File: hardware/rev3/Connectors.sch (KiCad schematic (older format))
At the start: 2 parts, among them J2 CONN_02X09, J3 CONN_02X09

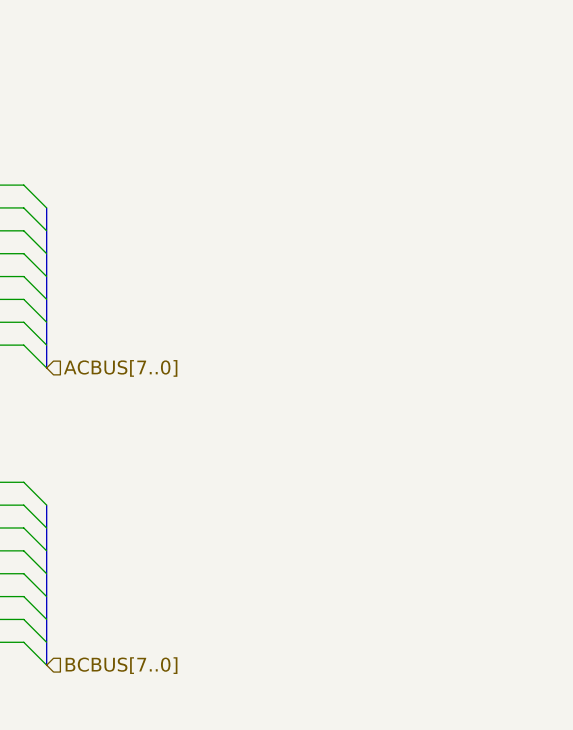
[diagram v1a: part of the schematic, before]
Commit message: Add initial output amplifier design.
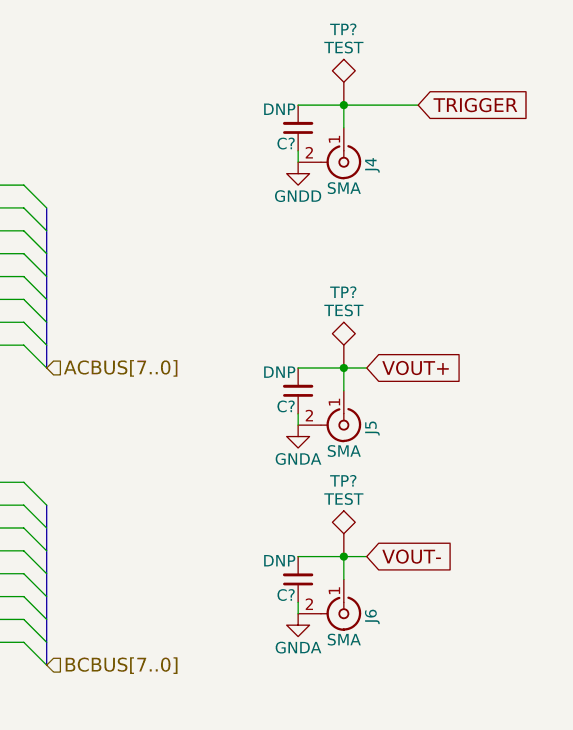
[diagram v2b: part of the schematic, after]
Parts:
- added C? (x3): DNP, symbol C_Small
- added J4, J5, J6: SMA, symbol CONN_COAXIAL
- added TP? (x3): TEST, symbol TEST
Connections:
- net GNDD: now also C?.1, J4.2 (Ext)
- new net GNDA: C?.1, C?.1, J5.2 (Ext), J6.2 (Ext)
- new net TRIGGER: C?.2, J4.1 (In), TP?.1
- new net VOUT+: C?.2, J5.1 (In), TP?.1
- new net VOUT-: C?.2, J6.1 (In), TP?.1
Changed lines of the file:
@@
 LIBS:transistors
 LIBS:conn
-LIBS:linear
 LIBS:regul
 LIBS:74xx
@@
 LIBS:AD9102
 LIBS:LMK61XX
+LIBS:linear
+LIBS:ltc6409
 LIBS:rev3-cache
 EELAYER 25 0
@@
 Text Label 2350 1350 0    60   ~ 0
 ACBUS0
+$Comp
+L CONN_COAXIAL J4
+U 1 1 58FD5BE5
+P 4250 1250
+F 0 "J4" H 4260 1370 50  0000 C CNN
+F 1 "SMA" V 4365 1250 50  0000 C CNN
+F 2 "" H 4250 1250 50  0001 C CNN
+F 3 "" H 4250 1250 50  0001 C CNN
+	1    4250 1250
+	0    1    1    0
+$EndComp
+$Comp
+L CONN_COAXIAL J5
+U 1 1 58FD5DAF
+P 4250 2400
+F 0 "J5" H 4260 2520 50  0000 C CNN
+F 1 "SMA" V 4365 2400 50  0000 C CNN
+F 2 "" H 4250 2400 50  0001 C CNN
+F 3 "" H 4250 2400 50  0001 C CNN
+	1    4250 2400
+	0    1    1    0
+$EndComp
+Text GLabel 4575 1000 2    60   Input ~ 0
+TRIGGER
+Wire Wire Line
+	4050 1000 4575 1000
+Wire Wire Line
+	4250 1000 4250 1100
+Text GLabel 4350 2150 2    60   Input ~ 0
+VOUT+
+Wire Wire Line
+	4050 2150 4350 2150
+Wire Wire Line
+	4250 2150 4250 2250
+$Comp
+L CONN_COAXIAL J6
+U 1 1 58FD62C2
+P 4250 3225
+F 0 "J6" H 4260 3345 50  0000 C CNN
+F 1 "SMA" V 4365 3225 50  0000 C CNN
+F 2 "" H 4250 3225 50  0001 C CNN
+F 3 "" H 4250 3225 50  0001 C CNN
+	1    4250 3225
+	0    1    1    0
+$EndComp
+Text GLabel 4350 2975 2    60   Input ~ 0
+VOUT-
+Wire Wire Line
+	4050 2975 4350 2975
+Wire Wire Line
+	4250 2975 4250 3075
+$Comp
+L GNDA #PWR022
+U 1 1 58FD6367
+P 4050 3225
+F 0 "#PWR022" H 4050 2975 50  0001 C CNN
+F 1 "GNDA" H 4050 3075 50  0000 C CNN
+F 2 "" H 4050 3225 50  0001 C CNN
+F 3 "" H 4050 3225 50  0001 C CNN
+	1    4050 3225
+	1    0    0    -1
+$EndComp
+$Comp
+L GNDA #PWR023
+U 1 1 58FD6388
+P 4050 2400
+F 0 "#PWR023" H 4050 2150 50  0001 C CNN
+F 1 "GNDA" H 4050 2250 50  0000 C CNN
+F 2 "" H 4050 2400 50  0001 C CNN
+F 3 "" H 4050 2400 50  0001 C CNN
+	1    4050 2400
+	1    0    0    -1
+$EndComp
+$Comp
+L GNDD #PWR024
+U 1 1 58FD63A4
+P 4050 1250
+F 0 "#PWR024" H 4050 1000 50  0001 C CNN
+F 1 "GNDD" H 4050 1100 50  0000 C CNN
+F 2 "" H 4050 1250 50  0001 C CNN
+F 3 "" H 4050 1250 50  0001 C CNN
+	1    4050 1250
+	1    0    0    -1
+$EndComp
+$Comp
+L TEST TP?
+U 1 1 58FE1411
+P 4250 1000
+F 0 "TP?" H 4250 1300 50  0000 C BNN
+F 1 "TEST" H 4250 1250 50  0000 C CNN
+F 2 "" H 4250 1000 50  0001 C CNN
+F 3 "" H 4250 1000 50  0001 C CNN
+	1    4250 1000
+	1    0    0    -1
+$EndComp
+$Comp
+L TEST TP?
+U 1 1 58FE14BE
+P 4250 2150
+F 0 "TP?" H 4250 2450 50  0000 C BNN
+F 1 "TEST" H 4250 2400 50  0000 C CNN
+F 2 "" H 4250 2150 50  0001 C CNN
+F 3 "" H 4250 2150 50  0001 C CNN
+	1    4250 2150
+	1    0    0    -1
+$EndComp
+$Comp
+L TEST TP?
+U 1 1 58FE152F
+P 4250 2975
+F 0 "TP?" H 4250 3275 50  0000 C BNN
+F 1 "TEST" H 4250 3225 50  0000 C CNN
+F 2 "" H 4250 2975 50  0001 C CNN
+F 3 "" H 4250 2975 50  0001 C CNN
+	1    4250 2975
+	1    0    0    -1
+$EndComp
+$Comp
+L C_Small C?
+U 1 1 58FE1669
+P 4050 3075
+F 0 "C?" H 4060 3145 50  0000 L CNN
+F 1 "DNP" H 4060 2995 50  0000 L CNN
+F 2 "" H 4050 3075 50  0001 C CNN
+F 3 "" H 4050 3075 50  0001 C CNN
+	1    4050 3075
+	-1   0    0    1
+$EndComp
+Connection ~ 4250 2975
+Wire Wire Line
+	4050 3175 4050 3225
+$Comp
+L C_Small C?
+U 1 1 58FE17E3
+P 4050 2250
+F 0 "C?" H 4060 2320 50  0000 L CNN
+F 1 "DNP" H 4060 2170 50  0000 L CNN
+F 2 "" H 4050 2250 50  0001 C CNN
+F 3 "" H 4050 2250 50  0001 C CNN
+	1    4050 2250
+	-1   0    0    1
+$EndComp
+Wire Wire Line
+	4050 2350 4050 2400
+Connection ~ 4250 2150
+$Comp
+L C_Small C?
+U 1 1 58FE19AD
+P 4050 1100
+F 0 "C?" H 4060 1170 50  0000 L CNN
+F 1 "DNP" H 4060 1020 50  0000 L CNN
+F 2 "" H 4050 1100 50  0001 C CNN
+F 3 "" H 4050 1100 50  0001 C CNN
+	1    4050 1100
+	-1   0    0    1
+$EndComp
+Connection ~ 4250 1000
+Wire Wire Line
+	4050 1200 4050 1250
 $EndSCHEMATC

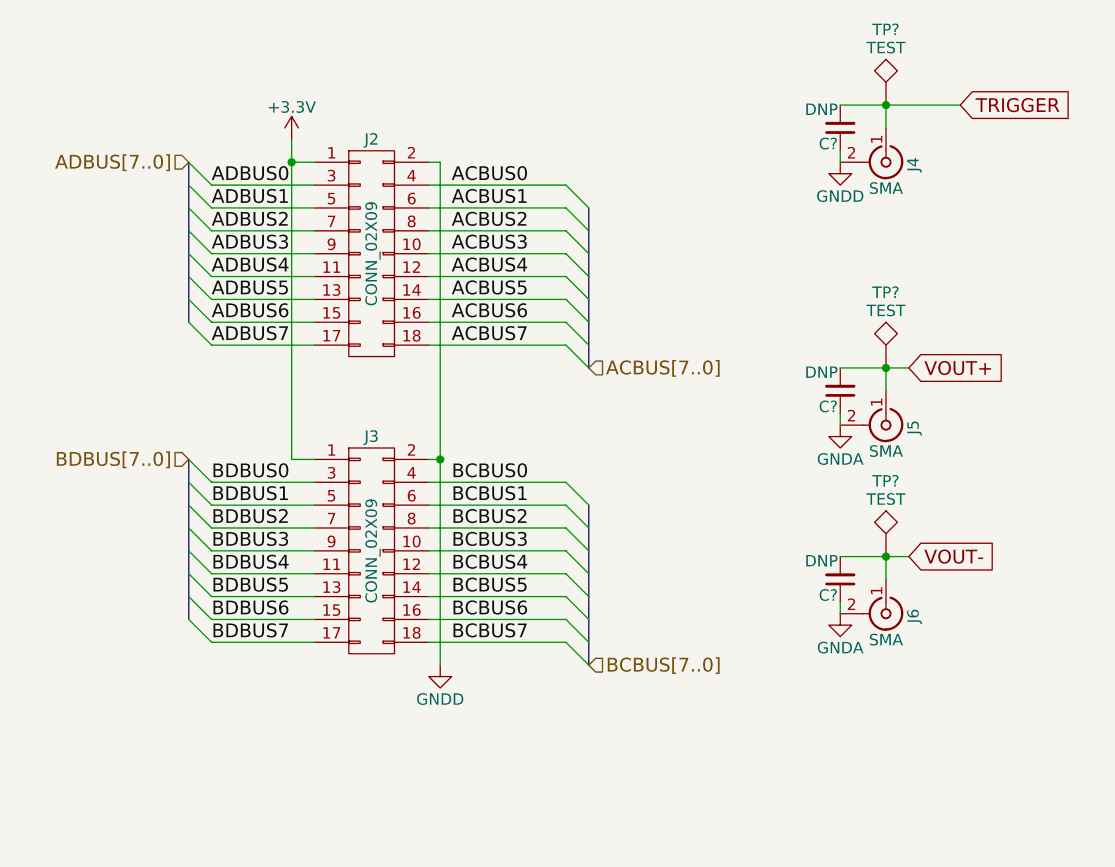
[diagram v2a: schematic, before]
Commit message: Finish up output amp schematic.
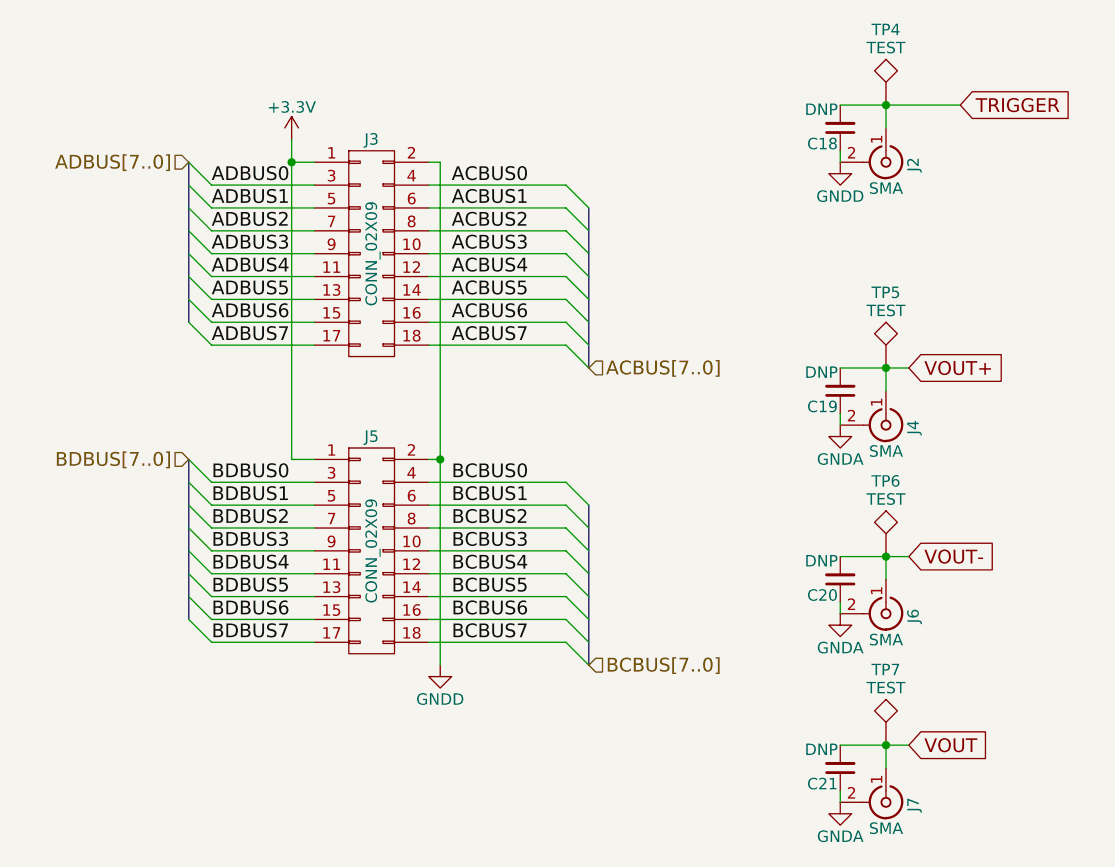
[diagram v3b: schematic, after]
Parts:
- added C21: DNP, symbol C_Small
- added J7: SMA, symbol CONN_COAXIAL
- added TP7: TEST, symbol TEST
- gave numbers to parts that had none: 6
- renumbered J4 to J2, J2 to J3, J5 to J4, J3 to J5
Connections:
- net GNDA: now also C21.1, J7.2 (Ext)
- new net VOUT: C21.2, J7.1 (In), TP7.1
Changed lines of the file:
@@
 LIBS:linear
 LIBS:ltc6409
+LIBS:ltc6269
 LIBS:rev3-cache
 EELAYER 25 0
@@
 $EndDescr
 $Comp
-L CONN_02X09 J2
+L CONN_02X09 J3
 U 1 1 58FB9080
 P 2000 1650
-F 0 "J2" H 2000 2150 50  0000 C CNN
+F 0 "J3" H 2000 2150 50  0000 C CNN
 F 1 "CONN_02X09" V 2000 1650 50  0000 C CNN
 F 2 "Pin_Headers:Pin_Header_Straight_2x09_Pitch2.54mm" H 2000 450 50  0001 C CNN
@@
 $EndComp
 $Comp
-L +3.3V #PWR020
+L +3.3V #PWR021
 U 1 1 58FB91A4
 P 1650 1150
-F 0 "#PWR020" H 1650 1000 50  0001 C CNN
+F 0 "#PWR021" H 1650 1000 50  0001 C CNN
 F 1 "+3.3V" H 1650 1290 50  0000 C CNN
 F 2 "" H 1650 1150 50  0001 C CNN
@@
 $EndComp
 $Comp
-L GNDD #PWR021
+L GNDD #PWR022
 U 1 1 58FB91BA
 P 2300 3450
-F 0 "#PWR021" H 2300 3200 50  0001 C CNN
+F 0 "#PWR022" H 2300 3200 50  0001 C CNN
 F 1 "GNDD" H 2300 3300 50  0000 C CNN
 F 2 "" H 2300 3450 50  0001 C CNN
@@
 	2250 1450 2850 1450
 $Comp
-L CONN_02X09 J3
+L CONN_02X09 J5
 U 1 1 58FB9420
 P 2000 2950
-F 0 "J3" H 2000 3450 50  0000 C CNN
+F 0 "J5" H 2000 3450 50  0000 C CNN
 F 1 "CONN_02X09" V 2000 2950 50  0000 C CNN
 F 2 "Pin_Headers:Pin_Header_Straight_2x09_Pitch2.54mm" H 2000 1750 50  0001 C CNN
@@
 ACBUS0
 $Comp
-L CONN_COAXIAL J4
+L CONN_COAXIAL J2
 U 1 1 58FD5BE5
 P 4250 1250
-F 0 "J4" H 4260 1370 50  0000 C CNN
+F 0 "J2" H 4260 1370 50  0000 C CNN
 F 1 "SMA" V 4365 1250 50  0000 C CNN
 F 2 "" H 4250 1250 50  0001 C CNN
@@
 $EndComp
 $Comp
-L CONN_COAXIAL J5
+L CONN_COAXIAL J4
 U 1 1 58FD5DAF
 P 4250 2400
-F 0 "J5" H 4260 2520 50  0000 C CNN
+F 0 "J4" H 4260 2520 50  0000 C CNN
 F 1 "SMA" V 4365 2400 50  0000 C CNN
 F 2 "" H 4250 2400 50  0001 C CNN
@@
 	4250 2975 4250 3075
 $Comp
-L GNDA #PWR022
+L GNDA #PWR023
 U 1 1 58FD6367
 P 4050 3225
-F 0 "#PWR022" H 4050 2975 50  0001 C CNN
+F 0 "#PWR023" H 4050 2975 50  0001 C CNN
 F 1 "GNDA" H 4050 3075 50  0000 C CNN
 F 2 "" H 4050 3225 50  0001 C CNN
@@
 $EndComp
 $Comp
-L GNDA #PWR023
+L GNDA #PWR024
 U 1 1 58FD6388
 P 4050 2400
-F 0 "#PWR023" H 4050 2150 50  0001 C CNN
+F 0 "#PWR024" H 4050 2150 50  0001 C CNN
 F 1 "GNDA" H 4050 2250 50  0000 C CNN
 F 2 "" H 4050 2400 50  0001 C CNN
@@
 $EndComp
 $Comp
-L GNDD #PWR024
+L GNDD #PWR025
 U 1 1 58FD63A4
 P 4050 1250
-F 0 "#PWR024" H 4050 1000 50  0001 C CNN
+F 0 "#PWR025" H 4050 1000 50  0001 C CNN
 F 1 "GNDD" H 4050 1100 50  0000 C CNN
 F 2 "" H 4050 1250 50  0001 C CNN
@@
 $EndComp
 $Comp
-L TEST TP?
+L TEST TP4
 U 1 1 58FE1411
 P 4250 1000
-F 0 "TP?" H 4250 1300 50  0000 C BNN
+F 0 "TP4" H 4250 1300 50  0000 C BNN
 F 1 "TEST" H 4250 1250 50  0000 C CNN
 F 2 "" H 4250 1000 50  0001 C CNN
@@
 $EndComp
 $Comp
-L TEST TP?
+L TEST TP5
 U 1 1 58FE14BE
 P 4250 2150
-F 0 "TP?" H 4250 2450 50  0000 C BNN
+F 0 "TP5" H 4250 2450 50  0000 C BNN
 F 1 "TEST" H 4250 2400 50  0000 C CNN
 F 2 "" H 4250 2150 50  0001 C CNN
@@
 $EndComp
 $Comp
-L TEST TP?
+L TEST TP6
 U 1 1 58FE152F
 P 4250 2975
-F 0 "TP?" H 4250 3275 50  0000 C BNN
+F 0 "TP6" H 4250 3275 50  0000 C BNN
 F 1 "TEST" H 4250 3225 50  0000 C CNN
 F 2 "" H 4250 2975 50  0001 C CNN
@@
 $EndComp
 $Comp
-L C_Small C?
+L C_Small C20
 U 1 1 58FE1669
 P 4050 3075
-F 0 "C?" H 4060 3145 50  0000 L CNN
+F 0 "C20" H 4060 3145 50  0000 L CNN
 F 1 "DNP" H 4060 2995 50  0000 L CNN
 F 2 "" H 4050 3075 50  0001 C CNN
@@
 	4050 3175 4050 3225
 $Comp
-L C_Small C?
+L C_Small C19
 U 1 1 58FE17E3
 P 4050 2250
-F 0 "C?" H 4060 2320 50  0000 L CNN
+F 0 "C19" H 4060 2320 50  0000 L CNN
 F 1 "DNP" H 4060 2170 50  0000 L CNN
 F 2 "" H 4050 2250 50  0001 C CNN
@@
 Connection ~ 4250 2150
 $Comp
-L C_Small C?
+L C_Small C18
 U 1 1 58FE19AD
 P 4050 1100
-F 0 "C?" H 4060 1170 50  0000 L CNN
+F 0 "C18" H 4060 1170 50  0000 L CNN
 F 1 "DNP" H 4060 1020 50  0000 L CNN
 F 2 "" H 4050 1100 50  0001 C CNN
@@
 Wire Wire Line
 	4050 1200 4050 1250
+$Comp
+L CONN_COAXIAL J7
+U 1 1 5903D255
+P 4250 4050
+F 0 "J7" H 4260 4170 50  0000 C CNN
+F 1 "SMA" V 4365 4050 50  0000 C CNN
+F 2 "" H 4250 4050 50  0001 C CNN
+F 3 "" H 4250 4050 50  0001 C CNN
+	1    4250 4050
+	0    1    1    0
+$EndComp
+$Comp
+L GNDA #PWR026
+U 1 1 5903D591
+P 4050 4050
+F 0 "#PWR026" H 4050 3800 50  0001 C CNN
+F 1 "GNDA" H 4050 3900 50  0000 C CNN
+F 2 "" H 4050 4050 50  0001 C CNN
+F 3 "" H 4050 4050 50  0001 C CNN
+	1    4050 4050
+	1    0    0    -1
+$EndComp
+$Comp
+L C_Small C21
+U 1 1 5903D618
+P 4050 3900
+F 0 "C21" H 4060 3970 50  0000 L CNN
+F 1 "DNP" H 4060 3820 50  0000 L CNN
+F 2 "" H 4050 3900 50  0001 C CNN
+F 3 "" H 4050 3900 50  0001 C CNN
+	1    4050 3900
+	-1   0    0    1
+$EndComp
+Wire Wire Line
+	4050 4050 4050 4000
+Wire Wire Line
+	4050 3800 4350 3800
+Wire Wire Line
+	4250 3800 4250 3900
+$Comp
+L TEST TP7
+U 1 1 5903D926
+P 4250 3800
+F 0 "TP7" H 4250 4100 50  0000 C BNN
+F 1 "TEST" H 4250 4050 50  0000 C CNN
+F 2 "" H 4250 3800 50  0001 C CNN
+F 3 "" H 4250 3800 50  0001 C CNN
+	1    4250 3800
+	1    0    0    -1
+$EndComp
+Text GLabel 4350 3800 2    60   Input ~ 0
+VOUT
+Connection ~ 4250 3800
 $EndSCHEMATC

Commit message: Add missing footprints.
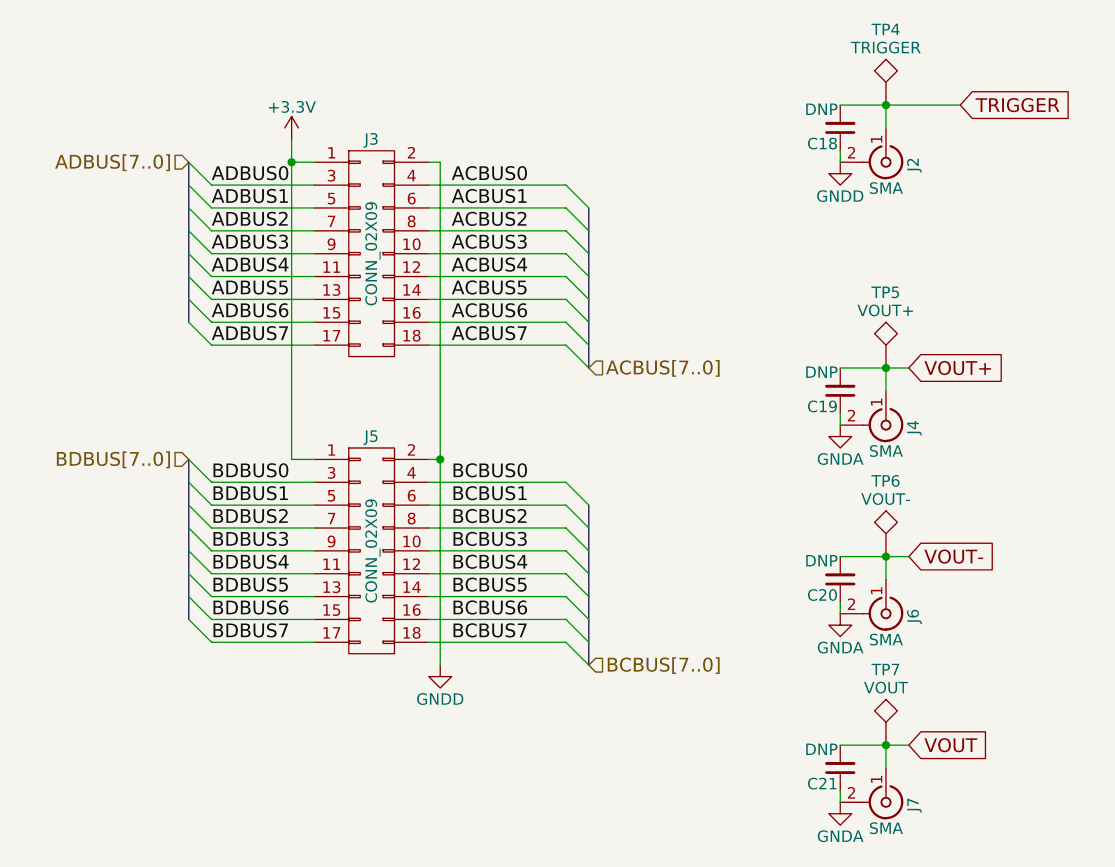
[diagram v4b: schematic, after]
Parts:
- C18, C19, C20, C21: footprint (none) -> Capacitors_SMD:C_0603_HandSoldering
- J2: footprint (none) -> Connectors:SMA_THT_Jack_Straight
- J4, J6, J7: footprint (none) -> Connectors_Molex:Molex_SMA_Jack_Edge_Mount
- TP4: value TEST -> TRIGGER; footprint (none) -> Measurement_Points:Test_Point_Keystone_5005-5009_Compact
- TP5: value TEST -> VOUT+; footprint (none) -> Measurement_Points:Test_Point_Keystone_5005-5009_Compact
- TP6: value TEST -> VOUT-; footprint (none) -> Measurement_Points:Test_Point_Keystone_5005-5009_Compact
- TP7: value TEST -> VOUT; footprint (none) -> Measurement_Points:Test_Point_Keystone_5005-5009_Compact
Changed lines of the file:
@@
 F 0 "J2" H 4260 1370 50  0000 C CNN
 F 1 "SMA" V 4365 1250 50  0000 C CNN
-F 2 "" H 4250 1250 50  0001 C CNN
+F 2 "Connectors:SMA_THT_Jack_Straight" H 4250 1250 50  0001 C CNN
 F 3 "" H 4250 1250 50  0001 C CNN
 	1    4250 1250
@@
 F 0 "J4" H 4260 2520 50  0000 C CNN
 F 1 "SMA" V 4365 2400 50  0000 C CNN
-F 2 "" H 4250 2400 50  0001 C CNN
+F 2 "Connectors_Molex:Molex_SMA_Jack_Edge_Mount" H 4250 2400 50  0001 C CNN
 F 3 "" H 4250 2400 50  0001 C CNN
 	1    4250 2400
@@
 F 0 "J6" H 4260 3345 50  0000 C CNN
 F 1 "SMA" V 4365 3225 50  0000 C CNN
-F 2 "" H 4250 3225 50  0001 C CNN
+F 2 "Connectors_Molex:Molex_SMA_Jack_Edge_Mount" H 4250 3225 50  0001 C CNN
 F 3 "" H 4250 3225 50  0001 C CNN
 	1    4250 3225
@@
 P 4250 1000
 F 0 "TP4" H 4250 1300 50  0000 C BNN
-F 1 "TEST" H 4250 1250 50  0000 C CNN
-F 2 "" H 4250 1000 50  0001 C CNN
+F 1 "TRIGGER" H 4250 1250 50  0000 C CNN
+F 2 "Measurement_Points:Test_Point_Keystone_5005-5009_Compact" H 4250 1000 50  0001 C CNN
 F 3 "" H 4250 1000 50  0001 C CNN
 	1    4250 1000
@@
 P 4250 2150
 F 0 "TP5" H 4250 2450 50  0000 C BNN
-F 1 "TEST" H 4250 2400 50  0000 C CNN
-F 2 "" H 4250 2150 50  0001 C CNN
+F 1 "VOUT+" H 4250 2400 50  0000 C CNN
+F 2 "Measurement_Points:Test_Point_Keystone_5005-5009_Compact" H 4250 2150 50  0001 C CNN
 F 3 "" H 4250 2150 50  0001 C CNN
 	1    4250 2150
@@
 P 4250 2975
 F 0 "TP6" H 4250 3275 50  0000 C BNN
-F 1 "TEST" H 4250 3225 50  0000 C CNN
-F 2 "" H 4250 2975 50  0001 C CNN
+F 1 "VOUT-" H 4250 3225 50  0000 C CNN
+F 2 "Measurement_Points:Test_Point_Keystone_5005-5009_Compact" H 4250 2975 50  0001 C CNN
 F 3 "" H 4250 2975 50  0001 C CNN
 	1    4250 2975
@@
 F 0 "C20" H 4060 3145 50  0000 L CNN
 F 1 "DNP" H 4060 2995 50  0000 L CNN
-F 2 "" H 4050 3075 50  0001 C CNN
+F 2 "Capacitors_SMD:C_0603_HandSoldering" H 4050 3075 50  0001 C CNN
 F 3 "" H 4050 3075 50  0001 C CNN
 	1    4050 3075
@@
 F 0 "C19" H 4060 2320 50  0000 L CNN
 F 1 "DNP" H 4060 2170 50  0000 L CNN
-F 2 "" H 4050 2250 50  0001 C CNN
+F 2 "Capacitors_SMD:C_0603_HandSoldering" H 4050 2250 50  0001 C CNN
 F 3 "" H 4050 2250 50  0001 C CNN
 	1    4050 2250
@@
 F 0 "C18" H 4060 1170 50  0000 L CNN
 F 1 "DNP" H 4060 1020 50  0000 L CNN
-F 2 "" H 4050 1100 50  0001 C CNN
+F 2 "Capacitors_SMD:C_0603_HandSoldering" H 4050 1100 50  0001 C CNN
 F 3 "" H 4050 1100 50  0001 C CNN
 	1    4050 1100
@@
 F 0 "J7" H 4260 4170 50  0000 C CNN
 F 1 "SMA" V 4365 4050 50  0000 C CNN
-F 2 "" H 4250 4050 50  0001 C CNN
+F 2 "Connectors_Molex:Molex_SMA_Jack_Edge_Mount" H 4250 4050 50  0001 C CNN
 F 3 "" H 4250 4050 50  0001 C CNN
 	1    4250 4050
@@
 F 0 "C21" H 4060 3970 50  0000 L CNN
 F 1 "DNP" H 4060 3820 50  0000 L CNN
-F 2 "" H 4050 3900 50  0001 C CNN
+F 2 "Capacitors_SMD:C_0603_HandSoldering" H 4050 3900 50  0001 C CNN
 F 3 "" H 4050 3900 50  0001 C CNN
 	1    4050 3900
@@
 P 4250 3800
 F 0 "TP7" H 4250 4100 50  0000 C BNN
-F 1 "TEST" H 4250 4050 50  0000 C CNN
-F 2 "" H 4250 3800 50  0001 C CNN
+F 1 "VOUT" H 4250 4050 50  0000 C CNN
+F 2 "Measurement_Points:Test_Point_Keystone_5005-5009_Compact" H 4250 3800 50  0001 C CNN
 F 3 "" H 4250 3800 50  0001 C CNN
 	1    4250 3800
